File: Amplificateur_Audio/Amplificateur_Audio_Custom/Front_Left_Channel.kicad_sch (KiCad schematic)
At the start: 78 parts, among them J701 Front Left Tweeter+, J702 Front Left Tweeter-, J703 Front Left Woofer+, J704 Front Left Woofer-, U701 PCM5252RHBR, U702 TPA3244DDWR

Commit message: Assignation des composants et empreintes terminé
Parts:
- removed J701: Front Left Tweeter+, symbol Connector:Conn_01x01_Pin
- removed J702: Front Left Tweeter-, symbol Connector:Conn_01x01_Pin
- removed J703: Front Left Woofer+, symbol Connector:Conn_01x01_Pin
- removed J704: Front Left Woofer-, symbol Connector:Conn_01x01_Pin
- added J705: Front Left Tweeter+, NewLibrary:630661MouserReel, symbol Connector:Conn_01x01_Pin
- added J706: Front Left Tweeter-, NewLibrary:630661MouserReel, symbol Connector:Conn_01x01_Pin
- added J707: Front Left Woofer+, NewLibrary:630661MouserReel, symbol Connector:Conn_01x01_Pin
- added J708: Front Left Woofer-, NewLibrary:630661MouserReel, symbol Connector:Conn_01x01_Pin
- C701, C702, C705, C716, C717, C718, C719, C720, C721, C722, C723, C724, C725, C732, C733, C734, C735, C736, C741, C742, C743, C744: footprint (none) -> Capacitor_SMD:C_0603_1608Metric_Pad1.08x0.95mm_HandSolder
- C703, C704, C706, C707, C708, C709, C710, C711: footprint (none) -> Capacitor_SMD:C_0402_1005Metric_Pad0.74x0.62mm_HandSolder
- C712, C713, C714, C715, C726, C727, C728, C729, C730, C731: footprint (none) -> Capacitor_SMD:C_1206_3216Metric_Pad1.33x1.80mm_HandSolder
- C737, C738, C739, C740: footprint (none) -> Capacitor_SMD:C_1210_3225Metric_Pad1.33x2.70mm_HandSolder
- JP701, JP702, JP703, JP704: footprint (none) -> Connector_PinHeader_2.54mm:PinHeader_1x03_P2.54mm_Vertical_SMD_Pin1Left
- L701: footprint (none) -> Inductor_SMD:L_0603_1608Metric_Pad1.05x0.95mm_HandSolder
- L702, L703: footprint (none) -> NewLibrary:UA8014ALD
- R701, R709, R710, R711, R712, R713, R714, R715, R716, R717, R718, R719, R720, R721: footprint (none) -> Resistor_SMD:R_0603_1608Metric_Pad0.98x0.95mm_HandSolder
- R702, R705: value 4.99k -> 10k; footprint (none) -> Resistor_SMD:R_0402_1005Metric_Pad0.72x0.64mm_HandSolder; now not fitted
- R703: footprint (none) -> Resistor_SMD:R_0402_1005Metric_Pad0.72x0.64mm_HandSolder; now fitted
- R704: value 10k -> 4.99k; footprint (none) -> Resistor_SMD:R_0402_1005Metric_Pad0.72x0.64mm_HandSolder
- R706, R708: footprint (none) -> Resistor_SMD:R_0402_1005Metric_Pad0.72x0.64mm_HandSolder
- R707: value 10k -> 4.99k; footprint (none) -> Resistor_SMD:R_0402_1005Metric_Pad0.72x0.64mm_HandSolder; now fitted
- U701: footprint (none) -> Package_DFN_QFN:Texas_RHB0032E_VQFN-32-1EP_5x5mm_P0.5mm_EP3.45x3.45mm_ThermalVias
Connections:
- net 3.3V-2: now also C702.2, C704.2, R702.2, R705.2, R707.1, R708.2; no longer C701.2, C703.2, R703.2, R705.1, R706.1, R707.2
- net FLT+: now also J705.1 (Pin_1)
- net FLT-: now also J706.1 (Pin_1)
- net FLW+: now also J707.1 (Pin_1)
- net FLW-: now also J708.1 (Pin_1)
- net GND: now also C708.1, C725.2, R703.1, R706.1; no longer C708.2, C725.1, R702.1, R708.1
- net at U702.9 (AVDD): now also C725.1; no longer C725.2
- net at U701.24 (MS/MODE2): now also R707.2; no longer R705.2
- net at R701.1, U701.14 (AVDD): now also C701.2, C703.2; no longer C702.2, C704.2
- net at U701.1 (XSMT): now also R708.1; no longer R706.2
- net at U701.2 (LDOO): now also C708.2; no longer C708.1
- net at U701.23 (MODE1): now also R704.2; no longer R702.2
- new net: R702.1, R703.2, U701.32 (MISO(GPIO1)/ADR1/FMT)
- new net: R705.1, R706.2, U701.22 (GPIO2/ADR2/GPO)

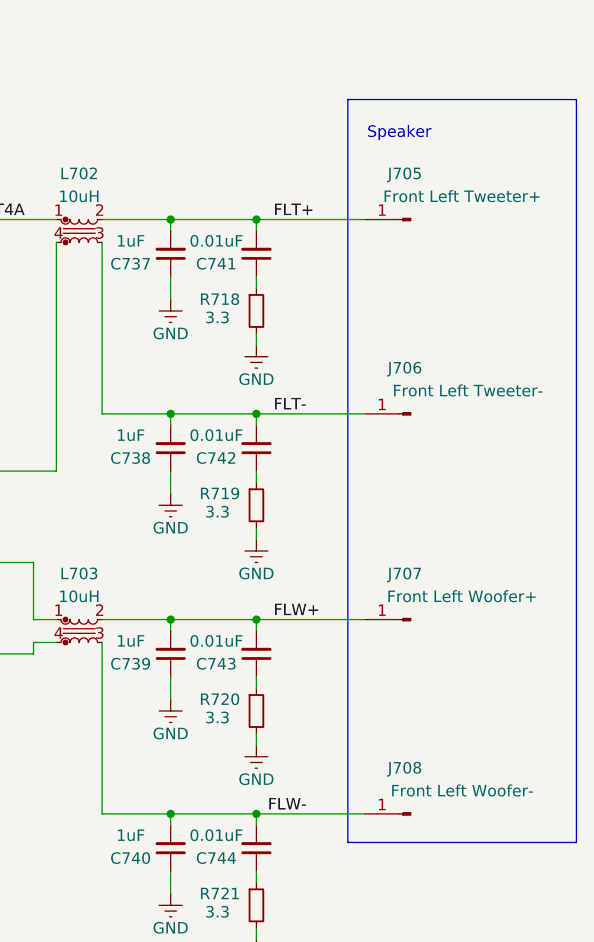
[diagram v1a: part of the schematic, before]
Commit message: Ajout de point de test et début du routage
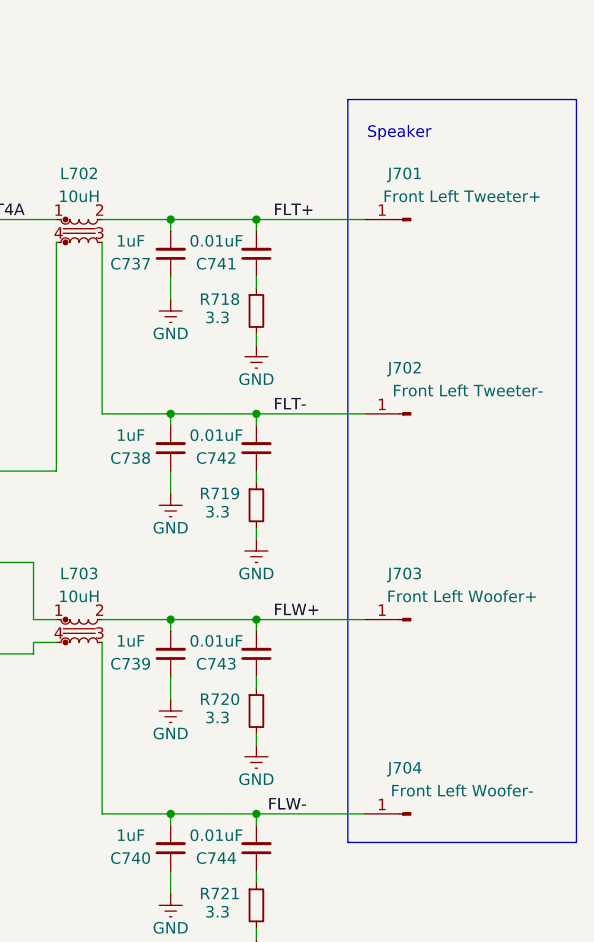
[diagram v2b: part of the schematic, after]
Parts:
- C730, C731: footprint Capacitor_SMD:C_1206_3216Metric_Pad1.33x1.80mm_HandSolder -> Capacitor_SMD:CP_Elec_16x17.5
- U702: footprint DDV0044D_N -> NewLibrary:DDV0044D_N
- renumbered J705 to J701, J706 to J702, J707 to J703, J708 to J704
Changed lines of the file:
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@@
 	)
 	(symbol
+		(lib_id "Device:C_Polarized_Small_US")
+		(at 272.415 73.66 0)
+		(unit 1)
+		(exclude_from_sim no)
+		(in_bom yes)
+		(on_board yes)
+		(dnp no)
+		(fields_autoplaced yes)
+		(property "Reference" "C730"
+			(at 274.955 71.9581 0)
+			(effects
+				(font
+					(size 1.27 1.27)
+				)
+				(justify left)
+			)
+		)
+		(property "Value" "1000uF"
+			(at 274.955 74.4981 0)
+			(effects
+				(font
+					(size 1.27 1.27)
+				)
+				(justify left)
+			)
+		)
+		(property "Footprint" "Capacitor_SMD:CP_Elec_16x17.5"
+			(at 272.415 73.66 0)
+			(effects
+				(font
+					(size 1.27 1.27)
+				)
+				(hide yes)
+			)
+		)
+		(property "Datasheet" "~"
+			(at 272.415 73.66 0)
+			(effects
+				(font
+					(size 1.27 1.27)
+				)
+				(hide yes)
+			)
+		)
+		(property "Description" "EEV-FK1H102M"
+			(at 272.415 73.66 0)
+			(effects
+				(font
+					(size 1.27 1.27)
+				)
+				(hide yes)
+			)
+		)
+		(pin "1"
+		)
+		(pin "2"
+		)
+		(instances
+			(project "Amplificateur_Audio"
+				(path "/bf9cc67f-178f-4c8c-b6a6-249a1896d599/7a445999-a030-4ec8-8810-54be223b32bd"
+					(reference "C730")
+					(unit 1)
+				)
+			)
+		)
+	)
+	(symbol
 		(lib_id "Device:C_Small")
 		(at 244.475 224.79 90)
@@
 	)
 	(symbol
-		(lib_id "Device:C_Polarized_Small_US")
-		(at 278.765 92.71 0)
-		(unit 1)
-		(exclude_from_sim no)
-		(in_bom yes)
-		(on_board yes)
-		(dnp no)
-		(fields_autoplaced yes)
-		(property "Reference" "C731"
-			(at 281.305 91.0081 0)
-			(effects
-				(font
-					(size 1.27 1.27)
-				)
-				(justify left)
-			)
-		)
-		(property "Value" "1000uF"
-			(at 281.305 93.5481 0)
-			(effects
-				(font
-					(size 1.27 1.27)
-				)
-				(justify left)
-			)
-		)
-		(property "Footprint" "Capacitor_SMD:C_1206_3216Metric_Pad1.33x1.80mm_HandSolder"
-			(at 278.765 92.71 0)
-			(effects
-				(font
-					(size 1.27 1.27)
-				)
-				(hide yes)
-			)
-		)
-		(property "Datasheet" "~"
-			(at 278.765 92.71 0)
-			(effects
-				(font
-					(size 1.27 1.27)
-				)
-				(hide yes)
-			)
-		)
-		(property "Description" "GRM31MR71H105KA88L"
-			(at 278.765 92.71 0)
-			(effects
-				(font
-					(size 1.27 1.27)
-				)
-				(hide yes)
-			)
-		)
-		(pin "1"
-		)
-		(pin "2"
-		)
-		(instances
-			(project "Amplificateur_Audio"
-				(path "/bf9cc67f-178f-4c8c-b6a6-249a1896d599/7a445999-a030-4ec8-8810-54be223b32bd"
-					(reference "C731")
-					(unit 1)
-				)
-			)
-		)
-	)
-	(symbol
 		(lib_id "Device:C_Small")
 		(at 198.755 92.075 0)
@@
 		(on_board yes)
 		(dnp no)
-		(property "Reference" "J706"
+		(property "Reference" "J702"
 			(at 381 129.54 0)
 			(effects
@@
 			(project "Amplificateur_Audio"
 				(path "/bf9cc67f-178f-4c8c-b6a6-249a1896d599/7a445999-a030-4ec8-8810-54be223b32bd"
-					(reference "J706")
+					(reference "J702")
 					(unit 1)
 				)
@@
 		(on_board yes)
 		(dnp no)
-		(property "Reference" "J705"
+		(property "Reference" "J701"
 			(at 381 107.95 0)
 			(effects
@@
 			(project "Amplificateur_Audio"
 				(path "/bf9cc67f-178f-4c8c-b6a6-249a1896d599/7a445999-a030-4ec8-8810-54be223b32bd"
-					(reference "J705")
+					(reference "J701")
 					(unit 1)
 				)
@@
 			)
 		)
-		(property "Footprint" "DDV0044D_N"
+		(property "Footprint" "NewLibrary:DDV0044D_N"
 			(at 277.495 181.61 0)
 			(effects
@@
 		(on_board yes)
 		(dnp no)
-		(property "Reference" "J707"
+		(property "Reference" "J703"
 			(at 381 152.4 0)
 			(effects
@@
 			(project "Amplificateur_Audio"
 				(path "/bf9cc67f-178f-4c8c-b6a6-249a1896d599/7a445999-a030-4ec8-8810-54be223b32bd"
-					(reference "J707")
+					(reference "J703")
 					(unit 1)
 				)
@@
 	)
 	(symbol
-		(lib_id "power:+12V")
-		(at 211.455 139.7 0)
+		(lib_id "Device:C_Polarized_Small_US")
+		(at 278.765 92.71 0)
 		(unit 1)
 		(exclude_from_sim no)
@@
 		(on_board yes)
 		(dnp no)
-		(property "Reference" "#PWR01006"
-			(at 211.455 143.51 0)
+		(fields_autoplaced yes)
+		(property "Reference" "C731"
+			(at 281.305 91.0081 0)
 			(effects
 				(font
 					(size 1.27 1.27)
 				)
-				(hide yes)
+				(justify left)
 			)
 		)
-		(property "Value" "12V"
-			(at 211.201 136.398 0)
+		(property "Value" "1000uF"
+			(at 281.305 93.5481 0)
 			(effects
 				(font
 					(size 1.27 1.27)
 				)
+				(justify left)
 			)
 		)
-		(property "Footprint" ""
-			(at 211.455 139.7 0)
+		(property "Footprint" "Capacitor_SMD:CP_Elec_16x17.5"
+			(at 278.765 92.71 0)
 			(effects
 				(font
@@
 			)
 		)
-		(property "Datasheet" ""
-			(at 211.455 139.7 0)
+		(property "Datasheet" "~"
+			(at 278.765 92.71 0)
 			(effects
 				(font
@@
 			)
 		)
-		(property "Description" "Power symbol creates a global label with name \"+12V\""
-			(at 211.455 139.7 0)
+		(property "Description" "EEV-FK1H102M"
+			(at 278.765 92.71 0)
 			(effects
 				(font
@@
 		(pin "1"
 		)
+		(pin "2"
+		)
 		(instances
 			(project "Amplificateur_Audio"
 				(path "/bf9cc67f-178f-4c8c-b6a6-249a1896d599/7a445999-a030-4ec8-8810-54be223b32bd"
-					(reference "#PWR01006")
+					(reference "C731")
 					(unit 1)
 				)
@@
 	)
 	(symbol
-		(lib_id "power:Earth")
-		(at 354.965 187.96 0)
+		(lib_id "power:+12V")
+		(at 211.455 139.7 0)
 		(unit 1)
 		(exclude_from_sim no)
@@
 		(on_board yes)
 		(dnp no)
-		(property "Reference" "#PWR01035"
-			(at 354.965 194.31 0)
+		(property "Reference" "#PWR01006"
+			(at 211.455 143.51 0)
 			(effects
 				(font
@@
 			)
 		)
-		(property "Value" "GND"
-			(at 354.965 191.77 0)
+		(property "Value" "12V"
+			(at 211.201 136.398 0)
 			(effects
 				(font
@@
 		)
 		(property "Footprint" ""
-			(at 354.965 187.96 0)
+			(at 211.455 139.7 0)
 			(effects
 				(font
@@
 			)
 		)
-		(property "Datasheet" "~"
-			(at 354.965 187.96 0)
+		(property "Datasheet" ""
+			(at 211.455 139.7 0)
 			(effects
 				(font
@@
 			)
 		)
-		(property "Description" "Power symbol creates a global label with name \"Earth\""
-			(at 354.965 187.96 0)
+		(property "Description" "Power symbol creates a global label with name \"+12V\""
+			(at 211.455 139.7 0)
 			(effects
 				(font
@@
 			(project "Amplificateur_Audio"
 				(path "/bf9cc67f-178f-4c8c-b6a6-249a1896d599/7a445999-a030-4ec8-8810-54be223b32bd"
-					(reference "#PWR01035")
+					(reference "#PWR01006")
 					(unit 1)
 				)
@@
 	)
 	(symbol
-		(lib_id "Device:C_Small")
-		(at 245.745 160.02 270)
+		(lib_id "power:Earth")
+		(at 354.965 187.96 0)
 		(unit 1)
 		(exclude_from_sim no)
@@
 		(on_board yes)
 		(dnp no)
-		(property "Reference" "C724"
-			(at 249.809 156.464 90)
+		(property "Reference" "#PWR01035"
+			(at 354.965 194.31 0)
 			(effects
 				(font
 					(size 1.27 1.27)
 				)
+				(hide yes)
 			)
 		)
-		(property "Value" "1uF"
-			(at 250.063 158.242 90)
+		(property "Value" "GND"
+			(at 354.965 191.77 0)
 			(effects
 				(font
@@
 			)
 		)
-		(property "Footprint" "Capacitor_SMD:C_0603_1608Metric_Pad1.08x0.95mm_HandSolder"
-			(at 245.745 160.02 0)
+		(property "Footprint" ""
+			(at 354.965 187.96 0)
 			(effects
 				(font
@@
 		)
 		(property "Datasheet" "~"
-			(at 245.745 160.02 0)
+			(at 354.965 187.96 0)
 			(effects
 				(font
@@
 			)
 		)
-		(property "Description" "GRM188R71C105KA12D"
-			(at 245.745 160.02 0)
+		(property "Description" "Power symbol creates a global label with name \"Earth\""
+			(at 354.965 187.96 0)
 			(effects
 				(font
@@
 			)
 		)
-		(pin "2"
-		)
 		(pin "1"
 		)
@@
 			(project "Amplificateur_Audio"
 				(path "/bf9cc67f-178f-4c8c-b6a6-249a1896d599/7a445999-a030-4ec8-8810-54be223b32bd"
-					(reference "C724")
+					(reference "#PWR01035")
 					(unit 1)
 				)
@@
 	)
 	(symbol
-		(lib_id "Device:C_Polarized_Small_US")
-		(at 272.415 73.66 0)
+		(lib_id "Device:C_Small")
+		(at 245.745 160.02 270)
 		(unit 1)
 		(exclude_from_sim no)
@@
 		(on_board yes)
 		(dnp no)
-		(fields_autoplaced yes)
-		(property "Reference" "C730"
-			(at 274.955 71.9581 0)
+		(property "Reference" "C724"
+			(at 249.809 156.464 90)
 			(effects
 				(font
 					(size 1.27 1.27)
 				)
-				(justify left)
 			)
 		)
-		(property "Value" "1000uF"
-			(at 274.955 74.4981 0)
+		(property "Value" "1uF"
+			(at 250.063 158.242 90)
 			(effects
 				(font
 					(size 1.27 1.27)
 				)
-				(justify left)
 			)
 		)
-		(property "Footprint" "Capacitor_SMD:C_1206_3216Metric_Pad1.33x1.80mm_HandSolder"
-			(at 272.415 73.66 0)
+		(property "Footprint" "Capacitor_SMD:C_0603_1608Metric_Pad1.08x0.95mm_HandSolder"
+			(at 245.745 160.02 0)
 			(effects
 				(font
@@
 		)
 		(property "Datasheet" "~"
-			(at 272.415 73.66 0)
+			(at 245.745 160.02 0)
 			(effects
 				(font
@@
 			)
 		)
-		(property "Description" "GRM31MR71H105KA88L"
-			(at 272.415 73.66 0)
+		(property "Description" "GRM188R71C105KA12D"
+			(at 245.745 160.02 0)
 			(effects
 				(font
@@
 			)
 		)
-		(pin "1"
-		)
 		(pin "2"
 		)
+		(pin "1"
+		)
 		(instances
 			(project "Amplificateur_Audio"
 				(path "/bf9cc67f-178f-4c8c-b6a6-249a1896d599/7a445999-a030-4ec8-8810-54be223b32bd"
-					(reference "C730")
+					(reference "C724")
 					(unit 1)
 				)
@@
 		(on_board yes)
 		(dnp no)
-		(property "Reference" "J708"
+		(property "Reference" "J704"
 			(at 381 173.99 0)
 			(effects
@@
 			(project "Amplificateur_Audio"
 				(path "/bf9cc67f-178f-4c8c-b6a6-249a1896d599/7a445999-a030-4ec8-8810-54be223b32bd"
-					(reference "J708")
+					(reference "J704")
 					(unit 1)
 				)

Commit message: Refactor : hierarchical template channels for multichannel routing
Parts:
- removed JP701, JP702, JP703, JP704: Jumper_3_Open, Connector_PinHeader_2.54mm:PinHeader_1x03_P2.54mm_Vertical_SMD_Pin1Left, symbol Jumper:Jumper_3_Open
- added C724, C727: 0.1uF, Capacitor_SMD:C_0603_1608Metric, symbol Device:C_Small
- C701, C702, C705, C716, C717, C718, C719, C720, C721, C722, C723: footprint Capacitor_SMD:C_0603_1608Metric_Pad1.08x0.95mm_HandSolder -> Capacitor_SMD:C_0603_1608Metric
- C703, C704, C706, C709, C710, C711: footprint Capacitor_SMD:C_0402_1005Metric_Pad0.74x0.62mm_HandSolder -> Capacitor_SMD:C_0402_1005Metric
- C707: renamed from C708; footprint Capacitor_SMD:C_0402_1005Metric_Pad0.74x0.62mm_HandSolder -> Capacitor_SMD:C_0402_1005Metric
- C708: renamed from C707; footprint Capacitor_SMD:C_0402_1005Metric_Pad0.74x0.62mm_HandSolder -> Capacitor_SMD:C_0402_1005Metric
- C712, C713, C714, C715: footprint Capacitor_SMD:C_1206_3216Metric_Pad1.33x1.80mm_HandSolder -> Capacitor_SMD:C_1206_3216Metric
- C725: renamed from C724; footprint Capacitor_SMD:C_0603_1608Metric_Pad1.08x0.95mm_HandSolder -> Capacitor_SMD:C_0603_1608Metric
- C726: renamed from C725; footprint Capacitor_SMD:C_0603_1608Metric_Pad1.08x0.95mm_HandSolder -> Capacitor_SMD:C_0603_1608Metric
- C728: renamed from C726; footprint Capacitor_SMD:C_1206_3216Metric_Pad1.33x1.80mm_HandSolder -> Capacitor_SMD:C_1206_3216Metric
- C729: renamed from C727; footprint Capacitor_SMD:C_1206_3216Metric_Pad1.33x1.80mm_HandSolder -> Capacitor_SMD:C_1206_3216Metric
- C730: renamed from C728; footprint Capacitor_SMD:C_1206_3216Metric_Pad1.33x1.80mm_HandSolder -> Capacitor_SMD:C_1206_3216Metric
- C731: renamed from C729; footprint Capacitor_SMD:C_1206_3216Metric_Pad1.33x1.80mm_HandSolder -> Capacitor_SMD:C_1206_3216Metric
- C732: renamed from C730; footprint Capacitor_SMD:CP_Elec_16x17.5 -> NewLibrary:CAP_EEVFK1H102M
- C733: renamed from C731; footprint Capacitor_SMD:CP_Elec_16x17.5 -> NewLibrary:CAP_EEVFK1H102M
- C734: renamed from C732; footprint Capacitor_SMD:C_0603_1608Metric_Pad1.08x0.95mm_HandSolder -> Capacitor_SMD:C_0603_1608Metric
- C735: renamed from C733; footprint Capacitor_SMD:C_0603_1608Metric_Pad1.08x0.95mm_HandSolder -> Capacitor_SMD:C_0603_1608Metric
- C736: renamed from C734; footprint Capacitor_SMD:C_0603_1608Metric_Pad1.08x0.95mm_HandSolder -> Capacitor_SMD:C_0603_1608Metric
- C737: renamed from C735; footprint Capacitor_SMD:C_0603_1608Metric_Pad1.08x0.95mm_HandSolder -> Capacitor_SMD:C_0603_1608Metric
- C738: renamed from C736; footprint Capacitor_SMD:C_0603_1608Metric_Pad1.08x0.95mm_HandSolder -> Capacitor_SMD:C_0603_1608Metric
- C739: renamed from C737; footprint Capacitor_SMD:C_1210_3225Metric_Pad1.33x2.70mm_HandSolder -> Capacitor_SMD:C_1210_3225Metric
- C740: renamed from C738; footprint Capacitor_SMD:C_1210_3225Metric_Pad1.33x2.70mm_HandSolder -> Capacitor_SMD:C_1210_3225Metric
- C741: renamed from C739; footprint Capacitor_SMD:C_1210_3225Metric_Pad1.33x2.70mm_HandSolder -> Capacitor_SMD:C_1210_3225Metric
- C742: renamed from C740; footprint Capacitor_SMD:C_1210_3225Metric_Pad1.33x2.70mm_HandSolder -> Capacitor_SMD:C_1210_3225Metric
- C743: renamed from C741; footprint Capacitor_SMD:C_0603_1608Metric_Pad1.08x0.95mm_HandSolder -> Capacitor_SMD:C_0603_1608Metric
- C744: renamed from C742; footprint Capacitor_SMD:C_0603_1608Metric_Pad1.08x0.95mm_HandSolder -> Capacitor_SMD:C_0603_1608Metric
- C745: renamed from C743; footprint Capacitor_SMD:C_0603_1608Metric_Pad1.08x0.95mm_HandSolder -> Capacitor_SMD:C_0603_1608Metric
- C746: renamed from C744; footprint Capacitor_SMD:C_0603_1608Metric_Pad1.08x0.95mm_HandSolder -> Capacitor_SMD:C_0603_1608Metric
- R701, R713, R714, R715, R716, R717: footprint Resistor_SMD:R_0603_1608Metric_Pad0.98x0.95mm_HandSolder -> Resistor_SMD:R_0603_1608Metric
- R702, R703, R704, R705, R706, R707, R708: footprint Resistor_SMD:R_0402_1005Metric_Pad0.72x0.64mm_HandSolder -> Resistor_SMD:R_0402_1005Metric
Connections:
- net DAC4L+: now also C712.1
- net DAC4L-: now also C713.1
- net DAC4R+: now also C715.1
- net DAC4R-: now also C714.1
- net GND: now also C724.1, C727.1
- net PVDD: now also C724.2, C727.2
- net VNEG: now reaches C709.1, U701.9 (VNEG)
- net MODE2: now reaches R707.2, U701.24 (MS/MODE2)
- net DACF4L-: now reaches C713.2, R714.2
- net LDOO: now reaches C707.2, U701.2 (LDOO)
- net MODE1: now reaches R704.2, U701.23 (MODE1)
- net MISO: now reaches R702.1, R703.2, U701.32 (MISO(GPIO1)/ADR1/FMT)
- net AVDD: now reaches C701.2, C703.2, R701.1, U701.14 (AVDD)
- net DACF4L+: now reaches C712.2, R713.2
- net DACF4R+: now reaches C715.2, R716.2
- net XSMT: now reaches R708.1, U701.1 (XSMT)
- net ADR2: now reaches R705.1, R706.2, U701.22 (GPIO2/ADR2/GPO)
- net DACF4R-: now reaches C714.2, R715.2
- net CAPP: now reaches C708.1, U701.6 (CAPP)
- net CAPM: now reaches C708.2, U701.8 (CAPM)
- net INPUTA4 renamed INPUTL4+
- net INPUTB4 renamed INPUTL4-
- net INPUTC4 renamed INPUTR4-
- net INPUTD4 renamed INPUTR4+
- net OUTLN4 renamed OUTL4-
- net OUTLP4 renamed OUTL4+
- net OUTRN4 renamed OUTR4-
- net OUTRP4 renamed OUTR4+
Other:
- note removed: "FROM INPUT HEADER"
- moved on the sheet: C708, C720, C721, C722, C723, C725, C726, C728, C729, C730, C731, C732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
